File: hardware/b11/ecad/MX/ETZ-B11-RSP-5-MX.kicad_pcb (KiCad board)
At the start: 2 copper layers, 144.7 x 90.2 mm, 0 parts

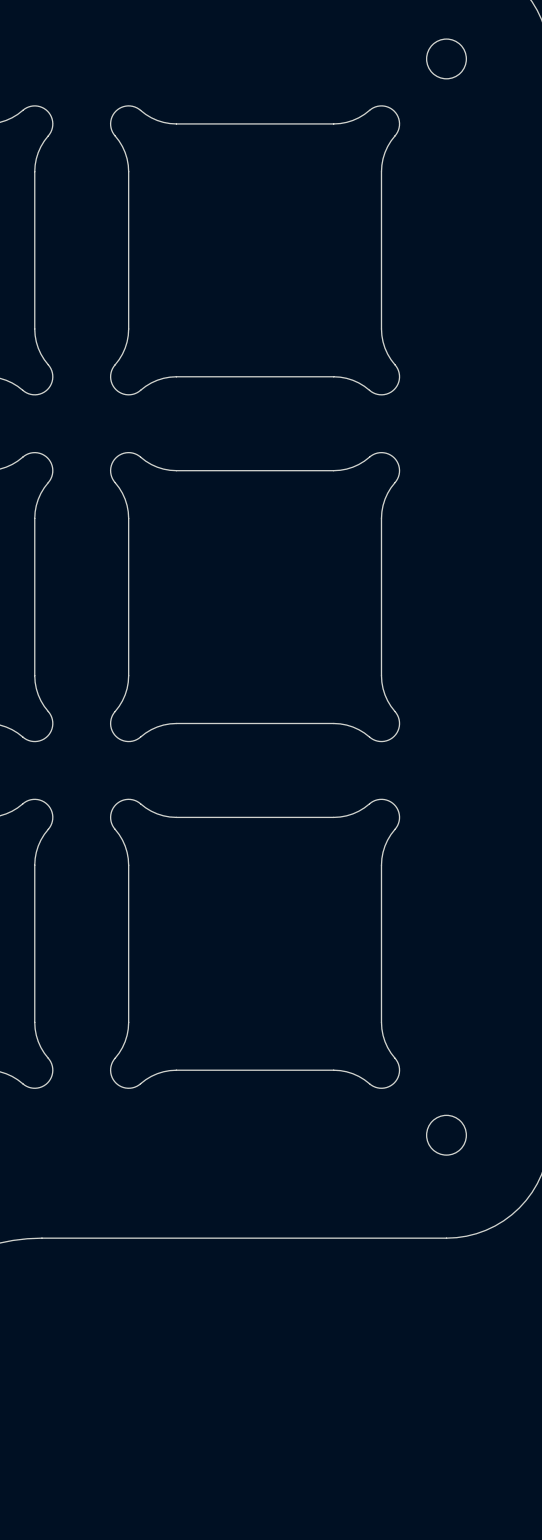
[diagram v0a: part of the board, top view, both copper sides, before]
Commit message: Add B11 display LED placement and stackups
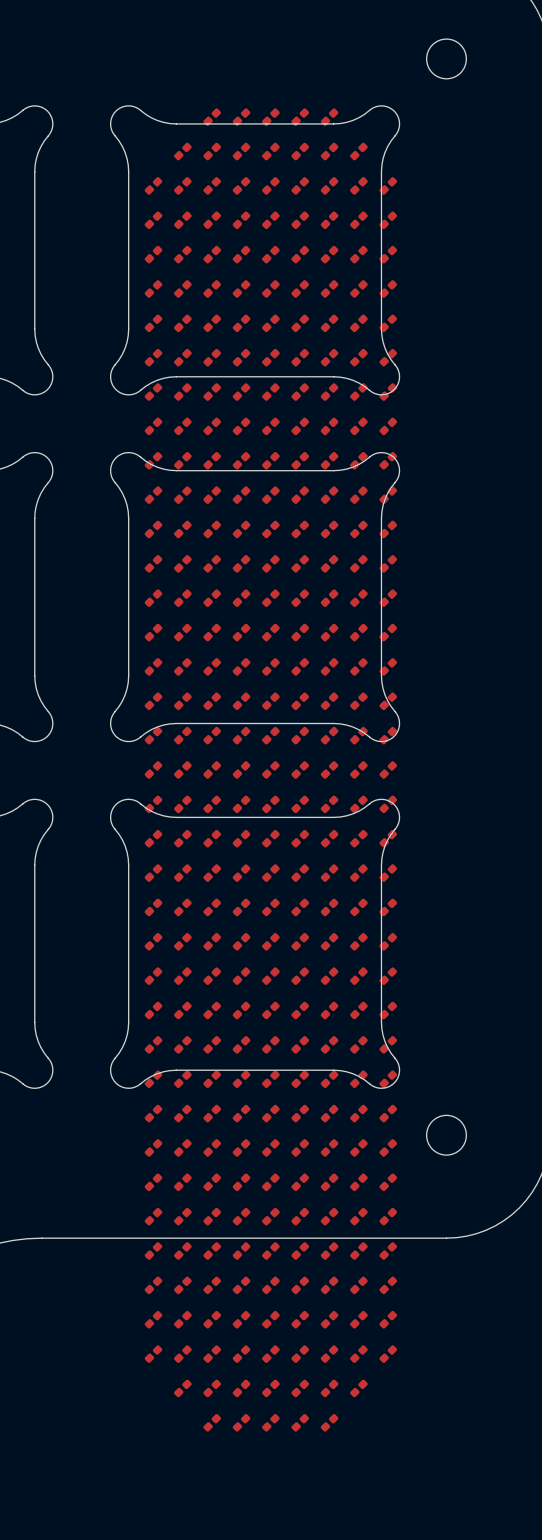
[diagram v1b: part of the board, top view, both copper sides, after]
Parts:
- added D1: 0201_LED, 0201_LED, F.Cu at (202.2, 68.1)
- added D10: 0201_LED, 0201_LED, F.Cu at (207.1, 70.0)
- added D100: 0201_LED, 0201_LED, F.Cu at (208.7, 89.1)
- added D101: 0201_LED, 0201_LED, F.Cu at (210.3, 89.1)
- added D102: 0201_LED, 0201_LED, F.Cu at (211.9, 89.1)
- added D103: 0201_LED, 0201_LED, F.Cu at (198.9, 91.0)
- added D104: 0201_LED, 0201_LED, F.Cu at (200.6, 91.0)
- added D105: 0201_LED, 0201_LED, F.Cu at (202.2, 91.0)
- added D106: 0201_LED, 0201_LED, F.Cu at (203.8, 91.0)
- added D107: 0201_LED, 0201_LED, F.Cu at (205.4, 91.0)
- added D108: 0201_LED, 0201_LED, F.Cu at (207.1, 91.0)
- added D109: 0201_LED, 0201_LED, F.Cu at (208.7, 91.0)
- added D11: 0201_LED, 0201_LED, F.Cu at (208.7, 70.0)
- added D110: 0201_LED, 0201_LED, F.Cu at (210.3, 91.0)
- added D111: 0201_LED, 0201_LED, F.Cu at (211.9, 91.0)
- added D112: 0201_LED, 0201_LED, F.Cu at (198.9, 92.9)
- added D113: 0201_LED, 0201_LED, F.Cu at (200.6, 92.9)
- added D114: 0201_LED, 0201_LED, F.Cu at (202.2, 92.9)
- added D115: 0201_LED, 0201_LED, F.Cu at (203.8, 92.9)
- added D116: 0201_LED, 0201_LED, F.Cu at (205.4, 92.9)
- added D117: 0201_LED, 0201_LED, F.Cu at (207.1, 92.9)
- added D118: 0201_LED, 0201_LED, F.Cu at (208.7, 92.9)
- added D119: 0201_LED, 0201_LED, F.Cu at (210.3, 92.9)
- added D12: 0201_LED, 0201_LED, F.Cu at (210.3, 70.0)
- added D120: 0201_LED, 0201_LED, F.Cu at (211.9, 92.9)
- added D121: 0201_LED, 0201_LED, F.Cu at (198.9, 94.8)
- added D122: 0201_LED, 0201_LED, F.Cu at (200.6, 94.8)
- added D123: 0201_LED, 0201_LED, F.Cu at (202.2, 94.8)
- added D124: 0201_LED, 0201_LED, F.Cu at (203.8, 94.8)
- added D125: 0201_LED, 0201_LED, F.Cu at (205.4, 94.8)
- added D126: 0201_LED, 0201_LED, F.Cu at (207.1, 94.8)
- added D127: 0201_LED, 0201_LED, F.Cu at (208.7, 94.8)
- added D128: 0201_LED, 0201_LED, F.Cu at (210.3, 94.8)
- added D129: 0201_LED, 0201_LED, F.Cu at (211.9, 94.8)
- added D13: 0201_LED, 0201_LED, F.Cu at (198.9, 71.9)
- added D130: 0201_LED, 0201_LED, F.Cu at (198.9, 96.7)
- added D131: 0201_LED, 0201_LED, F.Cu at (200.6, 96.7)
- added D132: 0201_LED, 0201_LED, F.Cu at (202.2, 96.7)
- added D133: 0201_LED, 0201_LED, F.Cu at (203.8, 96.7)
- added D134: 0201_LED, 0201_LED, F.Cu at (205.4, 96.7)
- added D135: 0201_LED, 0201_LED, F.Cu at (207.1, 96.7)
- added D136: 0201_LED, 0201_LED, F.Cu at (208.7, 96.7)
- added D137: 0201_LED, 0201_LED, F.Cu at (210.3, 96.7)
- added D138: 0201_LED, 0201_LED, F.Cu at (211.9, 96.7)
- added D139: 0201_LED, 0201_LED, F.Cu at (198.9, 98.6)
- added D14: 0201_LED, 0201_LED, F.Cu at (200.6, 71.9)
- added D140: 0201_LED, 0201_LED, F.Cu at (200.6, 98.6)
- added D141: 0201_LED, 0201_LED, F.Cu at (202.2, 98.6)
- added D142: 0201_LED, 0201_LED, F.Cu at (203.8, 98.6)
- added D143: 0201_LED, 0201_LED, F.Cu at (205.4, 98.6)
- added D144: 0201_LED, 0201_LED, F.Cu at (207.1, 98.6)
- added D145: 0201_LED, 0201_LED, F.Cu at (208.7, 98.6)
- added D146: 0201_LED, 0201_LED, F.Cu at (210.3, 98.6)
- added D147: 0201_LED, 0201_LED, F.Cu at (211.9, 98.6)
- added D148: 0201_LED, 0201_LED, F.Cu at (198.9, 100.5)
- added D149: 0201_LED, 0201_LED, F.Cu at (200.6, 100.5)
- added D15: 0201_LED, 0201_LED, F.Cu at (202.2, 71.9)
- added D150: 0201_LED, 0201_LED, F.Cu at (202.2, 100.5)
- added D151: 0201_LED, 0201_LED, F.Cu at (203.8, 100.5)
- added D152: 0201_LED, 0201_LED, F.Cu at (205.4, 100.5)
- added D153: 0201_LED, 0201_LED, F.Cu at (207.1, 100.5)
- added D154: 0201_LED, 0201_LED, F.Cu at (208.7, 100.5)
- added D155: 0201_LED, 0201_LED, F.Cu at (210.3, 100.5)
- added D156: 0201_LED, 0201_LED, F.Cu at (211.9, 100.5)
- added D157: 0201_LED, 0201_LED, F.Cu at (198.9, 102.4)
- added D158: 0201_LED, 0201_LED, F.Cu at (200.6, 102.4)
- added D159: 0201_LED, 0201_LED, F.Cu at (202.2, 102.4)
- added D16: 0201_LED, 0201_LED, F.Cu at (203.8, 71.9)
- added D160: 0201_LED, 0201_LED, F.Cu at (203.8, 102.4)
- added D161: 0201_LED, 0201_LED, F.Cu at (205.4, 102.4)
- added D162: 0201_LED, 0201_LED, F.Cu at (207.1, 102.4)
- added D163: 0201_LED, 0201_LED, F.Cu at (208.7, 102.4)
- added D164: 0201_LED, 0201_LED, F.Cu at (210.3, 102.4)
- added D165: 0201_LED, 0201_LED, F.Cu at (211.9, 102.4)
- added D166: 0201_LED, 0201_LED, F.Cu at (198.9, 104.3)
- added D167: 0201_LED, 0201_LED, F.Cu at (200.6, 104.3)
- added D168: 0201_LED, 0201_LED, F.Cu at (202.2, 104.3)
- added D169: 0201_LED, 0201_LED, F.Cu at (203.8, 104.3)
- added D17: 0201_LED, 0201_LED, F.Cu at (205.4, 71.9)
- added D170: 0201_LED, 0201_LED, F.Cu at (205.4, 104.3)
- added D171: 0201_LED, 0201_LED, F.Cu at (207.1, 104.3)
- added D172: 0201_LED, 0201_LED, F.Cu at (208.7, 104.3)
- added D173: 0201_LED, 0201_LED, F.Cu at (210.3, 104.3)
- added D174: 0201_LED, 0201_LED, F.Cu at (211.9, 104.3)
- added D175: 0201_LED, 0201_LED, F.Cu at (198.9, 106.2)
- added D176: 0201_LED, 0201_LED, F.Cu at (200.6, 106.2)
- added D177: 0201_LED, 0201_LED, F.Cu at (202.2, 106.2)
- added D178: 0201_LED, 0201_LED, F.Cu at (203.8, 106.2)
- added D179: 0201_LED, 0201_LED, F.Cu at (205.4, 106.2)
- added D18: 0201_LED, 0201_LED, F.Cu at (207.1, 71.9)
- added D180: 0201_LED, 0201_LED, F.Cu at (207.1, 106.2)
- added D181: 0201_LED, 0201_LED, F.Cu at (208.7, 106.2)
- added D182: 0201_LED, 0201_LED, F.Cu at (210.3, 106.2)
- added D183: 0201_LED, 0201_LED, F.Cu at (211.9, 106.2)
- added D184: 0201_LED, 0201_LED, F.Cu at (198.9, 108.1)
- added D185: 0201_LED, 0201_LED, F.Cu at (200.6, 108.1)
- added D186: 0201_LED, 0201_LED, F.Cu at (202.2, 108.1)
- added D187: 0201_LED, 0201_LED, F.Cu at (203.8, 108.1)
- added D188: 0201_LED, 0201_LED, F.Cu at (205.4, 108.1)
- added D189: 0201_LED, 0201_LED, F.Cu at (207.1, 108.1)
- added D19: 0201_LED, 0201_LED, F.Cu at (208.7, 71.9)
- added D190: 0201_LED, 0201_LED, F.Cu at (208.7, 108.1)
- added D191: 0201_LED, 0201_LED, F.Cu at (210.3, 108.1)
- added D192: 0201_LED, 0201_LED, F.Cu at (211.9, 108.1)
- added D193: 0201_LED, 0201_LED, F.Cu at (198.9, 110.0)
- added D194: 0201_LED, 0201_LED, F.Cu at (200.6, 110.0)
- added D195: 0201_LED, 0201_LED, F.Cu at (202.2, 110.0)
- added D196: 0201_LED, 0201_LED, F.Cu at (203.8, 110.0)
- added D197: 0201_LED, 0201_LED, F.Cu at (205.4, 110.0)
- added D198: 0201_LED, 0201_LED, F.Cu at (207.1, 110.0)
- added D199: 0201_LED, 0201_LED, F.Cu at (208.7, 110.0)
- added D2: 0201_LED, 0201_LED, F.Cu at (203.8, 68.1)
- added D20: 0201_LED, 0201_LED, F.Cu at (210.3, 71.9)
- added D200: 0201_LED, 0201_LED, F.Cu at (210.3, 110.0)
- added D201: 0201_LED, 0201_LED, F.Cu at (211.9, 110.0)
- added D202: 0201_LED, 0201_LED, F.Cu at (198.9, 111.9)
- added D203: 0201_LED, 0201_LED, F.Cu at (200.6, 111.9)
- added D204: 0201_LED, 0201_LED, F.Cu at (202.2, 111.9)
- added D205: 0201_LED, 0201_LED, F.Cu at (203.8, 111.9)
- added D206: 0201_LED, 0201_LED, F.Cu at (205.4, 111.9)
- added D207: 0201_LED, 0201_LED, F.Cu at (207.1, 111.9)
- added D208: 0201_LED, 0201_LED, F.Cu at (208.7, 111.9)
- added D209: 0201_LED, 0201_LED, F.Cu at (210.3, 111.9)
- added D21: 0201_LED, 0201_LED, F.Cu at (211.9, 71.9)
- added D210: 0201_LED, 0201_LED, F.Cu at (211.9, 111.9)
- added D211: 0201_LED, 0201_LED, F.Cu at (198.9, 113.8)
- added D212: 0201_LED, 0201_LED, F.Cu at (200.6, 113.8)
- added D213: 0201_LED, 0201_LED, F.Cu at (202.2, 113.8)
- added D214: 0201_LED, 0201_LED, F.Cu at (203.8, 113.8)
- added D215: 0201_LED, 0201_LED, F.Cu at (205.4, 113.8)
- added D216: 0201_LED, 0201_LED, F.Cu at (207.1, 113.8)
- added D217: 0201_LED, 0201_LED, F.Cu at (208.7, 113.8)
- added D218: 0201_LED, 0201_LED, F.Cu at (210.3, 113.8)
- added D219: 0201_LED, 0201_LED, F.Cu at (211.9, 113.8)
- added D22: 0201_LED, 0201_LED, F.Cu at (198.9, 73.8)
- added D220: 0201_LED, 0201_LED, F.Cu at (198.9, 115.7)
- added D221: 0201_LED, 0201_LED, F.Cu at (200.6, 115.7)
- added D222: 0201_LED, 0201_LED, F.Cu at (202.2, 115.7)
- added D223: 0201_LED, 0201_LED, F.Cu at (203.8, 115.7)
- added D224: 0201_LED, 0201_LED, F.Cu at (205.4, 115.7)
- added D225: 0201_LED, 0201_LED, F.Cu at (207.1, 115.7)
- added D226: 0201_LED, 0201_LED, F.Cu at (208.7, 115.7)
- added D227: 0201_LED, 0201_LED, F.Cu at (210.3, 115.7)
- added D228: 0201_LED, 0201_LED, F.Cu at (211.9, 115.7)
- added D229: 0201_LED, 0201_LED, F.Cu at (198.9, 117.6)
- added D23: 0201_LED, 0201_LED, F.Cu at (200.6, 73.8)
- added D230: 0201_LED, 0201_LED, F.Cu at (200.6, 117.6)
- added D231: 0201_LED, 0201_LED, F.Cu at (202.2, 117.6)
- added D232: 0201_LED, 0201_LED, F.Cu at (203.8, 117.6)
- added D233: 0201_LED, 0201_LED, F.Cu at (205.4, 117.6)
- added D234: 0201_LED, 0201_LED, F.Cu at (207.1, 117.6)
- added D235: 0201_LED, 0201_LED, F.Cu at (208.7, 117.6)
- added D236: 0201_LED, 0201_LED, F.Cu at (210.3, 117.6)
- added D237: 0201_LED, 0201_LED, F.Cu at (211.9, 117.6)
- added D238: 0201_LED, 0201_LED, F.Cu at (198.9, 119.5)
- added D239: 0201_LED, 0201_LED, F.Cu at (200.6, 119.5)
- added D24: 0201_LED, 0201_LED, F.Cu at (202.2, 73.8)
- added D240: 0201_LED, 0201_LED, F.Cu at (202.2, 119.5)
- added D241: 0201_LED, 0201_LED, F.Cu at (203.8, 119.5)
- added D242: 0201_LED, 0201_LED, F.Cu at (205.4, 119.5)
- added D243: 0201_LED, 0201_LED, F.Cu at (207.1, 119.5)
- added D244: 0201_LED, 0201_LED, F.Cu at (208.7, 119.5)
- added D245: 0201_LED, 0201_LED, F.Cu at (210.3, 119.5)
- added D246: 0201_LED, 0201_LED, F.Cu at (211.9, 119.5)
- added D247: 0201_LED, 0201_LED, F.Cu at (198.9, 121.4)
- added D248: 0201_LED, 0201_LED, F.Cu at (200.6, 121.4)
- added D249: 0201_LED, 0201_LED, F.Cu at (202.2, 121.4)
- added D25: 0201_LED, 0201_LED, F.Cu at (203.8, 73.8)
- added D250: 0201_LED, 0201_LED, F.Cu at (203.8, 121.4)
- added D251: 0201_LED, 0201_LED, F.Cu at (205.4, 121.4)
- added D252: 0201_LED, 0201_LED, F.Cu at (207.1, 121.4)
- added D253: 0201_LED, 0201_LED, F.Cu at (208.7, 121.4)
- added D254: 0201_LED, 0201_LED, F.Cu at (210.3, 121.4)
- added D255: 0201_LED, 0201_LED, F.Cu at (211.9, 121.4)
- added D256: 0201_LED, 0201_LED, F.Cu at (198.9, 123.3)
- added D257: 0201_LED, 0201_LED, F.Cu at (200.6, 123.3)
- added D258: 0201_LED, 0201_LED, F.Cu at (202.2, 123.3)
- added D259: 0201_LED, 0201_LED, F.Cu at (203.8, 123.3)
- added D26: 0201_LED, 0201_LED, F.Cu at (205.4, 73.8)
- added D260: 0201_LED, 0201_LED, F.Cu at (205.4, 123.3)
- added D261: 0201_LED, 0201_LED, F.Cu at (207.1, 123.3)
- added D262: 0201_LED, 0201_LED, F.Cu at (208.7, 123.3)
- added D263: 0201_LED, 0201_LED, F.Cu at (210.3, 123.3)
- added D264: 0201_LED, 0201_LED, F.Cu at (211.9, 123.3)
- added D265: 0201_LED, 0201_LED, F.Cu at (198.9, 125.2)
- added D266: 0201_LED, 0201_LED, F.Cu at (200.6, 125.2)
- added D267: 0201_LED, 0201_LED, F.Cu at (202.2, 125.2)
- added D268: 0201_LED, 0201_LED, F.Cu at (203.8, 125.2)
- added D269: 0201_LED, 0201_LED, F.Cu at (205.4, 125.2)
- added D27: 0201_LED, 0201_LED, F.Cu at (207.1, 73.8)
- added D270: 0201_LED, 0201_LED, F.Cu at (207.1, 125.2)
- added D271: 0201_LED, 0201_LED, F.Cu at (208.7, 125.2)
- added D272: 0201_LED, 0201_LED, F.Cu at (210.3, 125.2)
- added D273: 0201_LED, 0201_LED, F.Cu at (211.9, 125.2)
- added D274: 0201_LED, 0201_LED, F.Cu at (198.9, 127.1)
- added D275: 0201_LED, 0201_LED, F.Cu at (200.6, 127.1)
- added D276: 0201_LED, 0201_LED, F.Cu at (202.2, 127.1)
- added D277: 0201_LED, 0201_LED, F.Cu at (203.8, 127.1)
- added D278: 0201_LED, 0201_LED, F.Cu at (205.4, 127.1)
- added D279: 0201_LED, 0201_LED, F.Cu at (207.1, 127.1)
- added D28: 0201_LED, 0201_LED, F.Cu at (208.7, 73.8)
- added D280: 0201_LED, 0201_LED, F.Cu at (208.7, 127.1)
- added D281: 0201_LED, 0201_LED, F.Cu at (210.3, 127.1)
- added D282: 0201_LED, 0201_LED, F.Cu at (211.9, 127.1)
- added D283: 0201_LED, 0201_LED, F.Cu at (198.9, 129.0)
- added D284: 0201_LED, 0201_LED, F.Cu at (200.6, 129.0)
- added D285: 0201_LED, 0201_LED, F.Cu at (202.2, 129.0)
- added D286: 0201_LED, 0201_LED, F.Cu at (203.8, 129.0)
- added D287: 0201_LED, 0201_LED, F.Cu at (205.4, 129.0)
- added D288: 0201_LED, 0201_LED, F.Cu at (207.1, 129.0)
- added D289: 0201_LED, 0201_LED, F.Cu at (208.7, 129.0)
- added D29: 0201_LED, 0201_LED, F.Cu at (210.3, 73.8)
- added D290: 0201_LED, 0201_LED, F.Cu at (210.3, 129.0)
- added D291: 0201_LED, 0201_LED, F.Cu at (211.9, 129.0)
- added D292: 0201_LED, 0201_LED, F.Cu at (198.9, 130.9)
- added D293: 0201_LED, 0201_LED, F.Cu at (200.6, 130.9)
- added D294: 0201_LED, 0201_LED, F.Cu at (202.2, 130.9)
- added D295: 0201_LED, 0201_LED, F.Cu at (203.8, 130.9)
- added D296: 0201_LED, 0201_LED, F.Cu at (205.4, 130.9)
- added D297: 0201_LED, 0201_LED, F.Cu at (207.1, 130.9)
- added D298: 0201_LED, 0201_LED, F.Cu at (208.7, 130.9)
- added D299: 0201_LED, 0201_LED, F.Cu at (210.3, 130.9)
- added D3: 0201_LED, 0201_LED, F.Cu at (205.4, 68.1)
- added D30: 0201_LED, 0201_LED, F.Cu at (211.9, 73.8)
- added D300: 0201_LED, 0201_LED, F.Cu at (211.9, 130.9)
- added D301: 0201_LED, 0201_LED, F.Cu at (198.9, 132.8)
- added D302: 0201_LED, 0201_LED, F.Cu at (200.6, 132.8)
- added D303: 0201_LED, 0201_LED, F.Cu at (202.2, 132.8)
- added D304: 0201_LED, 0201_LED, F.Cu at (203.8, 132.8)
- added D305: 0201_LED, 0201_LED, F.Cu at (205.4, 132.8)
- added D306: 0201_LED, 0201_LED, F.Cu at (207.1, 132.8)
- added D307: 0201_LED, 0201_LED, F.Cu at (208.7, 132.8)
- added D308: 0201_LED, 0201_LED, F.Cu at (210.3, 132.8)
- added D309: 0201_LED, 0201_LED, F.Cu at (211.9, 132.8)
- added D31: 0201_LED, 0201_LED, F.Cu at (198.9, 75.7)
- added D310: 0201_LED, 0201_LED, F.Cu at (198.9, 134.7)
- added D311: 0201_LED, 0201_LED, F.Cu at (200.6, 134.7)
- added D312: 0201_LED, 0201_LED, F.Cu at (202.2, 134.7)
- added D313: 0201_LED, 0201_LED, F.Cu at (203.8, 134.7)
- added D314: 0201_LED, 0201_LED, F.Cu at (205.4, 134.7)
- added D315: 0201_LED, 0201_LED, F.Cu at (207.1, 134.7)
- added D316: 0201_LED, 0201_LED, F.Cu at (208.7, 134.7)
- added D317: 0201_LED, 0201_LED, F.Cu at (210.3, 134.7)
- added D318: 0201_LED, 0201_LED, F.Cu at (211.9, 134.7)
- added D319: 0201_LED, 0201_LED, F.Cu at (198.9, 136.6)
- added D32: 0201_LED, 0201_LED, F.Cu at (200.6, 75.7)
- added D320: 0201_LED, 0201_LED, F.Cu at (200.6, 136.6)
- added D321: 0201_LED, 0201_LED, F.Cu at (202.2, 136.6)
- added D322: 0201_LED, 0201_LED, F.Cu at (203.8, 136.6)
- added D323: 0201_LED, 0201_LED, F.Cu at (205.4, 136.6)
- added D324: 0201_LED, 0201_LED, F.Cu at (207.1, 136.6)
- added D325: 0201_LED, 0201_LED, F.Cu at (208.7, 136.6)
- added D326: 0201_LED, 0201_LED, F.Cu at (210.3, 136.6)
- added D327: 0201_LED, 0201_LED, F.Cu at (211.9, 136.6)
- added D328: 0201_LED, 0201_LED, F.Cu at (200.6, 138.5)
- added D329: 0201_LED, 0201_LED, F.Cu at (202.2, 138.5)
- added D33: 0201_LED, 0201_LED, F.Cu at (202.2, 75.7)
- added D330: 0201_LED, 0201_LED, F.Cu at (203.8, 138.5)
- added D331: 0201_LED, 0201_LED, F.Cu at (205.4, 138.5)
- added D332: 0201_LED, 0201_LED, F.Cu at (207.1, 138.5)
- added D333: 0201_LED, 0201_LED, F.Cu at (208.7, 138.5)
- added D334: 0201_LED, 0201_LED, F.Cu at (210.3, 138.5)
- added D335: 0201_LED, 0201_LED, F.Cu at (202.2, 140.4)
- added D336: 0201_LED, 0201_LED, F.Cu at (203.8, 140.4)
- added D337: 0201_LED, 0201_LED, F.Cu at (205.4, 140.4)
- added D338: 0201_LED, 0201_LED, F.Cu at (207.1, 140.4)
- added D339: 0201_LED, 0201_LED, F.Cu at (208.7, 140.4)
- added D34: 0201_LED, 0201_LED, F.Cu at (203.8, 75.7)
- added D35: 0201_LED, 0201_LED, F.Cu at (205.4, 75.7)
- added D36: 0201_LED, 0201_LED, F.Cu at (207.1, 75.7)
- added D37: 0201_LED, 0201_LED, F.Cu at (208.7, 75.7)
- added D38: 0201_LED, 0201_LED, F.Cu at (210.3, 75.7)
- added D39: 0201_LED, 0201_LED, F.Cu at (211.9, 75.7)
- added D4: 0201_LED, 0201_LED, F.Cu at (207.1, 68.1)
- added D40: 0201_LED, 0201_LED, F.Cu at (198.9, 77.6)
- added D41: 0201_LED, 0201_LED, F.Cu at (200.6, 77.6)
- added D42: 0201_LED, 0201_LED, F.Cu at (202.2, 77.6)
- added D43: 0201_LED, 0201_LED, F.Cu at (203.8, 77.6)
- added D44: 0201_LED, 0201_LED, F.Cu at (205.4, 77.6)
- added D45: 0201_LED, 0201_LED, F.Cu at (207.1, 77.6)
- added D46: 0201_LED, 0201_LED, F.Cu at (208.7, 77.6)
- added D47: 0201_LED, 0201_LED, F.Cu at (210.3, 77.6)
- added D48: 0201_LED, 0201_LED, F.Cu at (211.9, 77.6)
- added D49: 0201_LED, 0201_LED, F.Cu at (198.9, 79.5)
- added D5: 0201_LED, 0201_LED, F.Cu at (208.7, 68.1)
- added D50: 0201_LED, 0201_LED, F.Cu at (200.6, 79.5)
- added D51: 0201_LED, 0201_LED, F.Cu at (202.2, 79.5)
- added D52: 0201_LED, 0201_LED, F.Cu at (203.8, 79.5)
- added D53: 0201_LED, 0201_LED, F.Cu at (205.4, 79.5)
- added D54: 0201_LED, 0201_LED, F.Cu at (207.1, 79.5)
- added D55: 0201_LED, 0201_LED, F.Cu at (208.7, 79.5)
- added D56: 0201_LED, 0201_LED, F.Cu at (210.3, 79.5)
- added D57: 0201_LED, 0201_LED, F.Cu at (211.9, 79.5)
- added D58: 0201_LED, 0201_LED, F.Cu at (198.9, 81.4)
- added D59: 0201_LED, 0201_LED, F.Cu at (200.6, 81.4)
- added D6: 0201_LED, 0201_LED, F.Cu at (200.6, 70.0)
- added D60: 0201_LED, 0201_LED, F.Cu at (202.2, 81.4)
- added D61: 0201_LED, 0201_LED, F.Cu at (203.8, 81.4)
- added D62: 0201_LED, 0201_LED, F.Cu at (205.4, 81.4)
- added D63: 0201_LED, 0201_LED, F.Cu at (207.1, 81.4)
- added D64: 0201_LED, 0201_LED, F.Cu at (208.7, 81.4)
- added D65: 0201_LED, 0201_LED, F.Cu at (210.3, 81.4)
- added D66: 0201_LED, 0201_LED, F.Cu at (211.9, 81.4)
- added D67: 0201_LED, 0201_LED, F.Cu at (198.9, 83.3)
- added D68: 0201_LED, 0201_LED, F.Cu at (200.6, 83.3)
- added D69: 0201_LED, 0201_LED, F.Cu at (202.2, 83.3)
- added D7: 0201_LED, 0201_LED, F.Cu at (202.2, 70.0)
- added D70: 0201_LED, 0201_LED, F.Cu at (203.8, 83.3)
- added D71: 0201_LED, 0201_LED, F.Cu at (205.4, 83.3)
- added D72: 0201_LED, 0201_LED, F.Cu at (207.1, 83.3)
- added D73: 0201_LED, 0201_LED, F.Cu at (208.7, 83.3)
- added D74: 0201_LED, 0201_LED, F.Cu at (210.3, 83.3)
- added D75: 0201_LED, 0201_LED, F.Cu at (211.9, 83.3)
- added D76: 0201_LED, 0201_LED, F.Cu at (198.9, 85.2)
- added D77: 0201_LED, 0201_LED, F.Cu at (200.6, 85.2)
- added D78: 0201_LED, 0201_LED, F.Cu at (202.2, 85.2)
- added D79: 0201_LED, 0201_LED, F.Cu at (203.8, 85.2)
- added D8: 0201_LED, 0201_LED, F.Cu at (203.8, 70.0)
- added D80: 0201_LED, 0201_LED, F.Cu at (205.4, 85.2)
- added D81: 0201_LED, 0201_LED, F.Cu at (207.1, 85.2)
- added D82: 0201_LED, 0201_LED, F.Cu at (208.7, 85.2)
- added D83: 0201_LED, 0201_LED, F.Cu at (210.3, 85.2)
- added D84: 0201_LED, 0201_LED, F.Cu at (211.9, 85.2)
- added D85: 0201_LED, 0201_LED, F.Cu at (198.9, 87.2)
- added D86: 0201_LED, 0201_LED, F.Cu at (200.6, 87.2)
- added D87: 0201_LED, 0201_LED, F.Cu at (202.2, 87.2)
- added D88: 0201_LED, 0201_LED, F.Cu at (203.8, 87.2)
- added D89: 0201_LED, 0201_LED, F.Cu at (205.4, 87.2)
- added D9: 0201_LED, 0201_LED, F.Cu at (205.4, 70.0)
- added D90: 0201_LED, 0201_LED, F.Cu at (207.1, 87.2)
- added D91: 0201_LED, 0201_LED, F.Cu at (208.7, 87.2)
- added D92: 0201_LED, 0201_LED, F.Cu at (210.3, 87.2)
- added D93: 0201_LED, 0201_LED, F.Cu at (211.9, 87.2)
- added D94: 0201_LED, 0201_LED, F.Cu at (198.9, 89.1)
- added D95: 0201_LED, 0201_LED, F.Cu at (200.6, 89.1)
- added D96: 0201_LED, 0201_LED, F.Cu at (202.2, 89.1)
- added D97: 0201_LED, 0201_LED, F.Cu at (203.8, 89.1)
- added D98: 0201_LED, 0201_LED, F.Cu at (205.4, 89.1)
- added D99: 0201_LED, 0201_LED, F.Cu at (207.1, 89.1)
